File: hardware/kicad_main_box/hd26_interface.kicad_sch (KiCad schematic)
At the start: 1 part, among them J1 HD26_FEMALE

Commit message: hardware(schematic): assign exact footprints to all hierarchical schematic symbols
- Assign SMD footprints for ESP32-S3, ES8388, TCAN334G, LM5164-Q1, TPS7A0533
- Assign footprints for Bourns LM-NP-1001 transformers, TLP222A PhotoMOS, TVS, passives, and IDC26 connector
- Fix F8 PCB netlist synchronization (0 unassigned footprint errors)
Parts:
- J1: footprint (none) -> Connector_IDC:IDC-Header_2x13_P2.54mm_Vertical
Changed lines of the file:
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@@
 		(property "Reference" "J1" (at 120.0 95.0 0) (effects (font (size 1.27 1.27))))
 		(property "Value" "HD26_FEMALE" (at 120.0 98.0 0) (effects (font (size 1.27 1.27))))
+		(property "Footprint" "Connector_IDC:IDC-Header_2x13_P2.54mm_Vertical" (at 0 0 0) (effects (font (size 1.27 1.27)) (hide yes)))
 		(pin "1")
 		(pin "2")

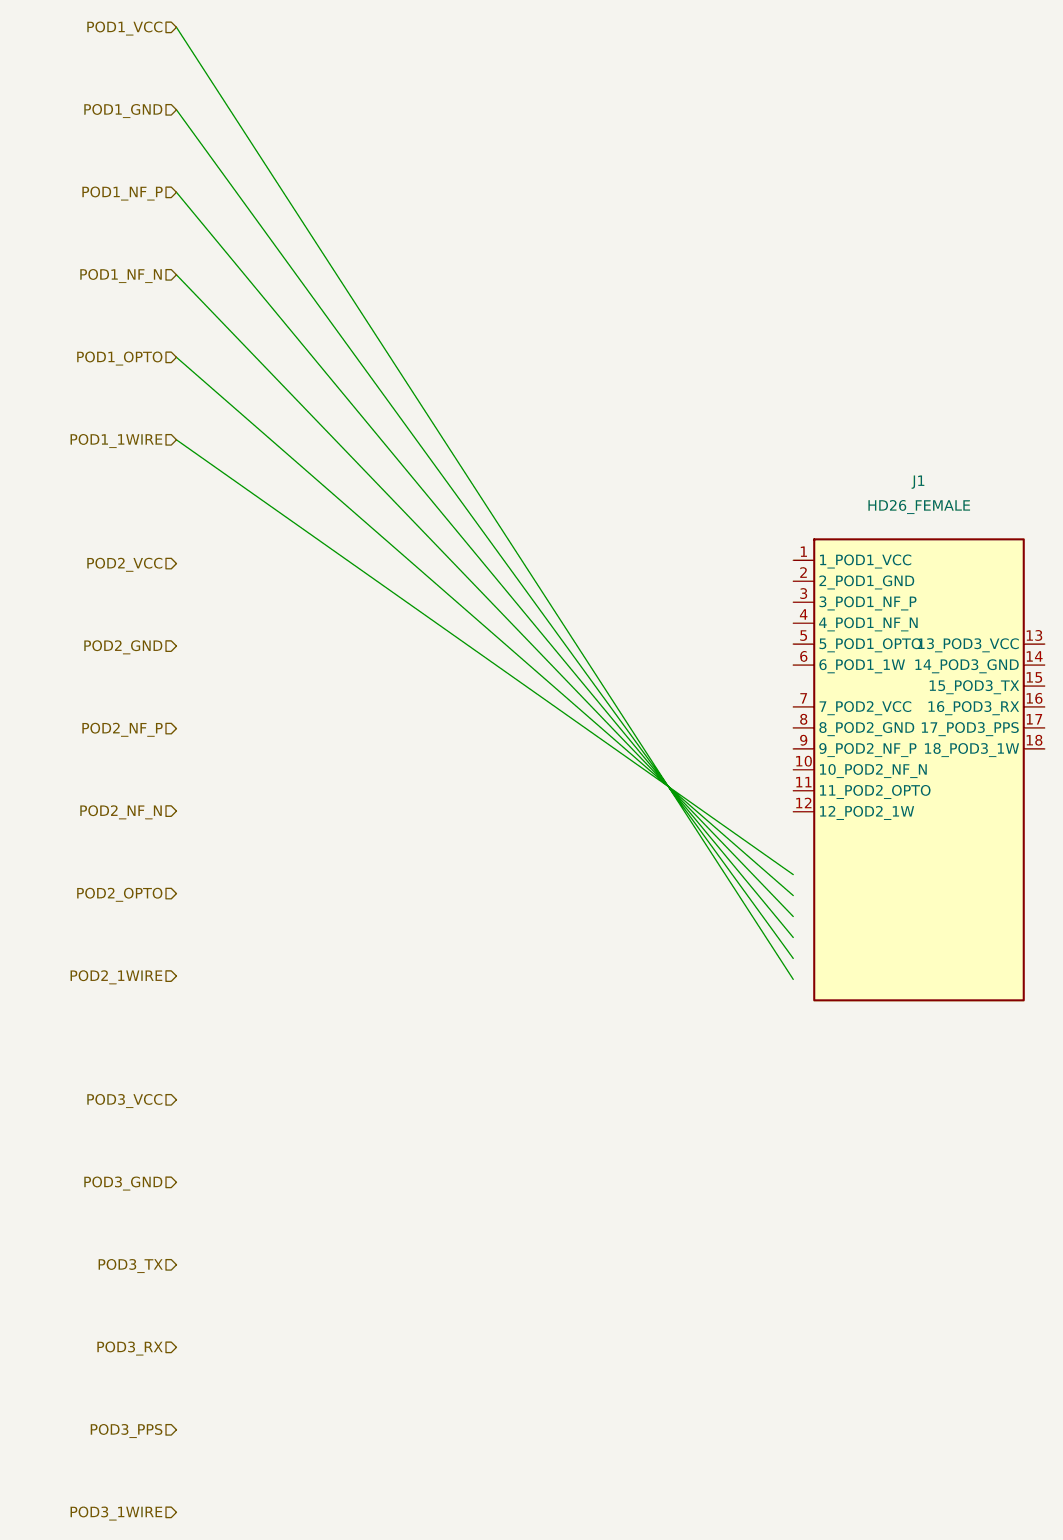
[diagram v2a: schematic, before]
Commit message: feat(arch): finalize v8.5/v9.0 Clean All-UWB Architecture, 6-PCBA lineup and Pure-DC wiring in documentation
- All-UWB Interconnects: Central Box communicates with Front-Node, Bay 1 (Left), Bay 2 (Right), and Rear Radar strictly over Qorvo DW3110 UWB (6.489 GHz Ch. 5, <0.4 ms latency, AES-128-CCM).
- Symmetrical Mounting Bays: Pod 1 and Pod 2 are physical docking bays (Bucht 1 / Bucht 2, Left / Right) for gateway units, NOT Fahrer / Sozius. Rider and pillion helmets connect directly via Bluetooth to Central Box DSP.
- 6-PCBA Lineup: PCBA 02 (Pod Base) and PCBA 04 (Rear Pod 3) retired and archived. Pod enclosures use direct 2-wire DC leaf spring contacts (+5V/GND). PCBA 03 is 2-sided SMT with DW3110, Host-MCU, and 4x AO3400A MOSFETs.
- Deutsch DTM-12 Harness: Replaced HD26 connector with 12-pin Deutsch DTM-12 automotive connector providing pure DC power.
- Power Sequencing & Roaming: Boot sequence (T=0, 200, 350, 500 ms), HW button SW1 (pairing & NVS reset), and 4-vehicle NVS roaming.
- Documentation Updated: docs/de/ 01, 03, 04, 07, 08, 09, 13, 14, 15, 16, status.md, DECISIONS_LOG.md (ADR-011), and hardware/README.md.
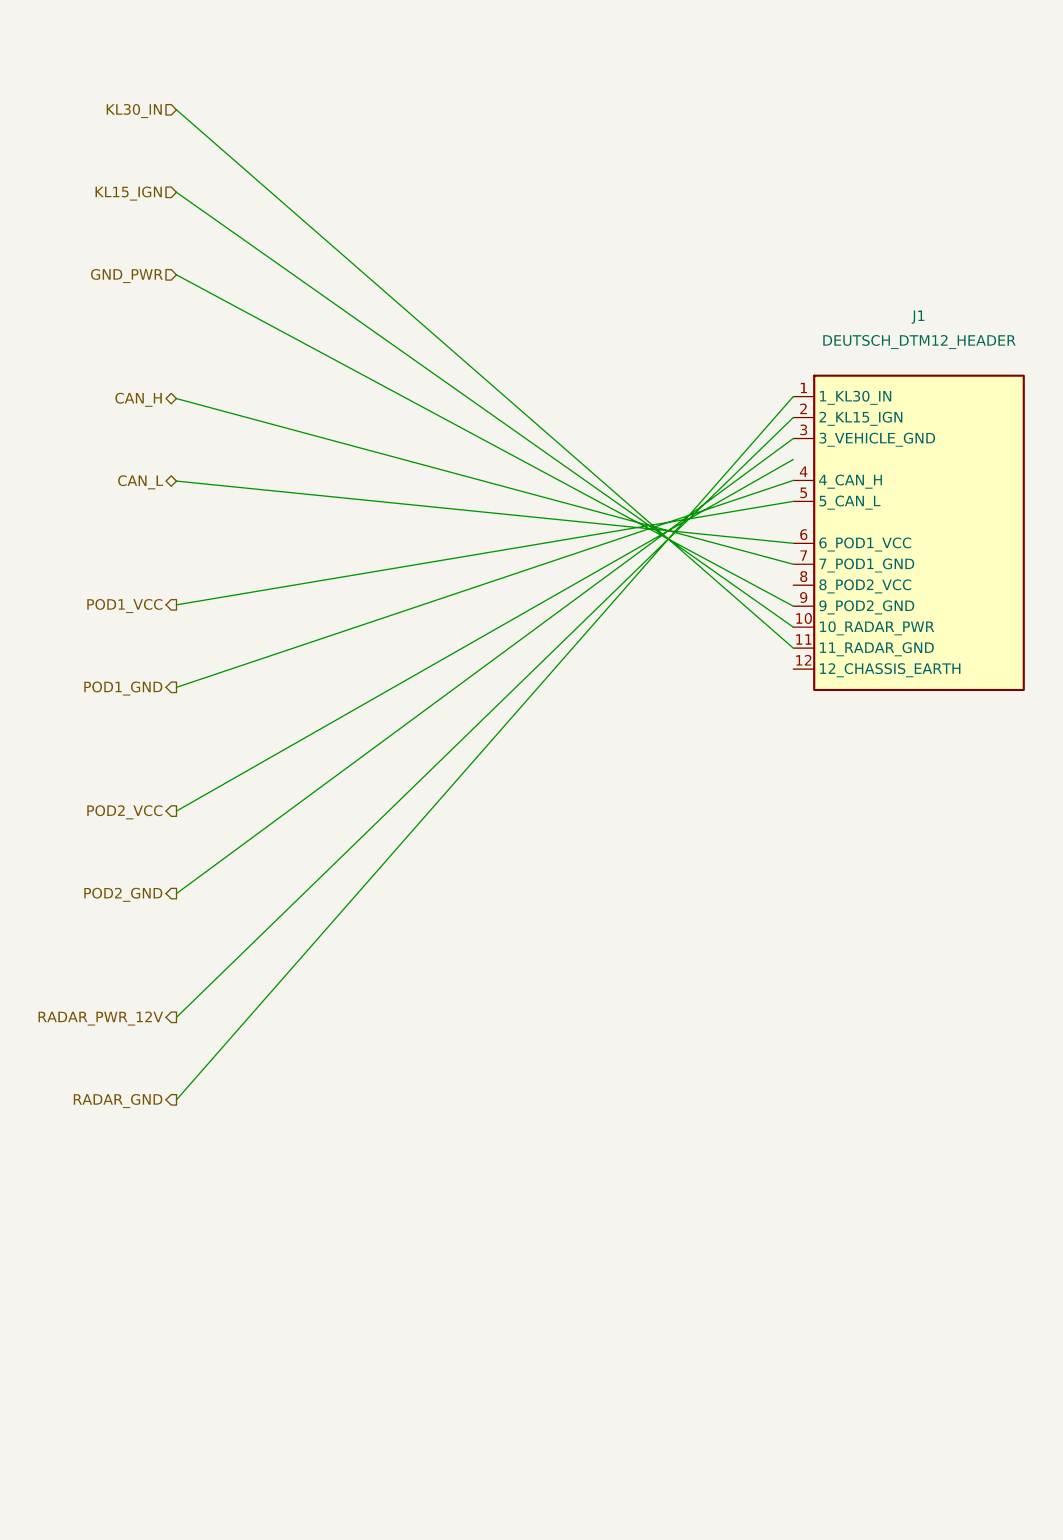
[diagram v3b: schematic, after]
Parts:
- J1: value HD26_FEMALE -> DEUTSCH_DTM12_HEADER; symbol Connector:HD26_Female -> Connector:Deutsch_DTM12_Male; LCSC (none) -> C2934175
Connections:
- net POD1_GND: now also J1.4 (4_CAN_H)
- net POD1_VCC: now also J1.5 (5_CAN_L)
- net POD2_GND: now also J1.3 (3_VEHICLE_GND)
- net RADAR_GND: now reaches J1.1 (1_KL30_IN)
- net KL15_IGN: now reaches J1.10 (10_RADAR_PWR)
- net KL30_IN: now reaches J1.11 (11_RADAR_GND)
- net RADAR_PWR_12V: now reaches J1.2 (2_KL15_IGN)
- net CAN_L: now reaches J1.6 (6_POD1_VCC)
- net CAN_H: now reaches J1.7 (7_POD1_GND)
- net GND_PWR: now reaches J1.9 (9_POD2_GND)
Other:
- title: OpenMotorBridge v8.0 - HD26 Matrix-Schnittstelle & Bordnetz -> OpenMotorBridge v8.5 / v9.0 - Deutsch DTM-12 Power & CAN Interface
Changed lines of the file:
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@@
 	(paper "A3")
 	(title_block
-		(title "OpenMotorBridge v8.0 - HD26 Matrix-Schnittstelle & Bordnetz")
-		(date "2026-08-24")
-		(rev "v8.0")
+		(title "OpenMotorBridge v8.5 / v9.0 - Deutsch DTM-12 Power & CAN Interface")
+		(date "2026-09-26")
+		(rev "v9.0")
 		(company "OpenMotorBridge Open Source Hardware")
-		(comment 1 "HD26 High-Density 26-Pin Industriesteckverbinder fuer alle externen Leitungen")
-		(comment 2 "Port 1 (Fahrer), Port 2 (Sozius), Port 3 (M8 Heck), KL30/KL15, CAN-Bus, Garmin Line-In")
+		(comment 1 "Deutsch DTM 12-Pin Automotive Industriestecker (Pure-DC & CAN)")
+		(comment 2 "KL30, KL15, GND, CAN-FD, 2x Pod 5V Power, Radar 12V Power; 100% UWB Wireless Data")
 	)
-	(hierarchical_label "POD1_VCC" (shape input) (at 30.0 40.0 180) (effects (font (size 1.27 1.27)) (justify right)))
-	(hierarchical_label "POD1_GND" (shape input) (at 30.0 50.0 180) (effects (font (size 1.27 1.27)) (justify right)))
-	(hierarchical_label "POD1_NF_P" (shape input) (at 30.0 60.0 180) (effects (font (size 1.27 1.27)) (justify right)))
-	(hierarchical_label "POD1_NF_N" (shape input) (at 30.0 70.0 180) (effects (font (size 1.27 1.27)) (justify right)))
-	(hierarchical_label "POD1_OPTO" (shape input) (at 30.0 80.0 180) (effects (font (size 1.27 1.27)) (justify right)))
-	(hierarchical_label "POD1_1WIRE" (shape input) (at 30.0 90.0 180) (effects (font (size 1.27 1.27)) (justify right)))
-	(hierarchical_label "POD2_VCC" (shape input) (at 30.0 105.0 180) (effects (font (size 1.27 1.27)) (justify right)))
-	(hierarchical_label "POD2_GND" (shape input) (at 30.0 115.0 180) (effects (font (size 1.27 1.27)) (justify right)))
-	(hierarchical_label "POD2_NF_P" (shape input) (at 30.0 125.0 180) (effects (font (size 1.27 1.27)) (justify right)))
-	(hierarchical_label "POD2_NF_N" (shape input) (at 30.0 135.0 180) (effects (font (size 1.27 1.27)) (justify right)))
-	(hierarchical_label "POD2_OPTO" (shape input) (at 30.0 145.0 180) (effects (font (size 1.27 1.27)) (justify right)))
-	(hierarchical_label "POD2_1WIRE" (shape input) (at 30.0 155.0 180) (effects (font (size 1.27 1.27)) (justify right)))
-	(hierarchical_label "POD3_VCC" (shape input) (at 30.0 170.0 180) (effects (font (size 1.27 1.27)) (justify right)))
-	(hierarchical_label "POD3_GND" (shape input) (at 30.0 180.0 180) (effects (font (size 1.27 1.27)) (justify right)))
-	(hierarchical_label "POD3_TX" (shape input) (at 30.0 190.0 180) (effects (font (size 1.27 1.27)) (justify right)))
-	(hierarchical_label "POD3_RX" (shape input) (at 30.0 200.0 180) (effects (font (size 1.27 1.27)) (justify right)))
-	(hierarchical_label "POD3_PPS" (shape input) (at 30.0 210.0 180) (effects (font (size 1.27 1.27)) (justify right)))
-	(hierarchical_label "POD3_1WIRE" (shape input) (at 30.0 220.0 180) (effects (font (size 1.27 1.27)) (justify right)))
-	(symbol (lib_id "Connector:HD26_Female") (at 120.0 130.0 0) (unit 1)
+	(hierarchical_label "KL30_IN" (shape input) (at 30.0 50.0 180) (effects (font (size 1.27 1.27)) (justify right)))
+	(hierarchical_label "KL15_IGN" (shape input) (at 30.0 60.0 180) (effects (font (size 1.27 1.27)) (justify right)))
+	(hierarchical_label "GND_PWR" (shape input) (at 30.0 70.0 180) (effects (font (size 1.27 1.27)) (justify right)))
+	(hierarchical_label "CAN_H" (shape bidirectional) (at 30.0 85.0 180) (effects (font (size 1.27 1.27)) (justify right)))
+	(hierarchical_label "CAN_L" (shape bidirectional) (at 30.0 95.0 180) (effects (font (size 1.27 1.27)) (justify right)))
+	(hierarchical_label "POD1_VCC" (shape output) (at 30.0 110.0 180) (effects (font (size 1.27 1.27)) (justify right)))
+	(hierarchical_label "POD1_GND" (shape output) (at 30.0 120.0 180) (effects (font (size 1.27 1.27)) (justify right)))
+	(hierarchical_label "POD2_VCC" (shape output) (at 30.0 135.0 180) (effects (font (size 1.27 1.27)) (justify right)))
+	(hierarchical_label "POD2_GND" (shape output) (at 30.0 145.0 180) (effects (font (size 1.27 1.27)) (justify right)))
+	(hierarchical_label "RADAR_PWR_12V" (shape output) (at 30.0 160.0 180) (effects (font (size 1.27 1.27)) (justify right)))
+	(hierarchical_label "RADAR_GND" (shape output) (at 30.0 170.0 180) (effects (font (size 1.27 1.27)) (justify right)))
+	(symbol (lib_id "Connector:Deutsch_DTM12_Male") (at 120.0 100.0 0) (unit 1)
 		(in_bom yes) (on_board yes) (dnp no)
-		(property "Reference" "J1" (at 120.0 95.0 0) (effects (font (size 1.27 1.27))))
-		(property "Value" "HD26_FEMALE" (at 120.0 98.0 0) (effects (font (size 1.27 1.27))))
+		(property "Reference" "J1" (at 120.0 75.0 0) (effects (font (size 1.27 1.27))))
+		(property "Value" "DEUTSCH_DTM12_HEADER" (at 120.0 78.0 0) (effects (font (size 1.27 1.27))))
 		(property "Footprint" "Connector_IDC:IDC-Header_2x13_P2.54mm_Vertical" (at 0 0 0) (effects (font (size 1.27 1.27)) (hide yes)))
+		(property "LCSC" "C2934175" (at 0 0 0) (effects (font (size 1.27 1.27)) (hide yes)))
 		(pin "1")
 		(pin "2")
@@
 		(pin "11")
 		(pin "12")
-		(pin "13")
-		(pin "14")
-		(pin "15")
-		(pin "16")
-		(pin "17")
-		(pin "18")
 	)
-	(wire (pts (xy 30.0 40.0) (xy 104.76 155.4)) (stroke (width 0) (type solid)))
-	(wire (pts (xy 30.0 50.0) (xy 104.76 152.86)) (stroke (width 0) (type solid)))
-	(wire (pts (xy 30.0 60.0) (xy 104.76 150.32)) (stroke (width 0) (type solid)))
-	(wire (pts (xy 30.0 70.0) (xy 104.76 147.78)) (stroke (width 0) (type solid)))
-	(wire (pts (xy 30.0 80.0) (xy 104.76 145.24)) (stroke (width 0) (type solid)))
-	(wire (pts (xy 30.0 90.0) (xy 104.76 142.7)) (stroke (width 0) (type solid)))
+	(wire (pts (xy 30.0 50.0) (xy 104.76 115.24)) (stroke (width 0) (type solid)))
+	(wire (pts (xy 30.0 60.0) (xy 104.76 112.70)) (stroke (width 0) (type solid)))
+	(wire (pts (xy 30.0 70.0) (xy 104.76 110.16)) (stroke (width 0) (type solid)))
+	(wire (pts (xy 30.0 85.0) (xy 104.76 105.08)) (stroke (width 0) (type solid)))
+	(wire (pts (xy 30.0 95.0) (xy 104.76 102.54)) (stroke (width 0) (type solid)))
+	(wire (pts (xy 30.0 110.0) (xy 104.76 97.46)) (stroke (width 0) (type solid)))
+	(wire (pts (xy 30.0 120.0) (xy 104.76 94.92)) (stroke (width 0) (type solid)))
+	(wire (pts (xy 30.0 135.0) (xy 104.76 92.38)) (stroke (width 0) (type solid)))
+	(wire (pts (xy 30.0 145.0) (xy 104.76 89.84)) (stroke (width 0) (type solid)))
+	(wire (pts (xy 30.0 160.0) (xy 104.76 87.30)) (stroke (width 0) (type solid)))
+	(wire (pts (xy 30.0 170.0) (xy 104.76 84.76)) (stroke (width 0) (type solid)))
 )

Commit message: hardware(pcb): synchronize 5-PCBA lineup with v9.6 All-UWB architecture
- PCBA 01 (Central Box): replace obsolete 26-pin IDC header with 12-pin Deutsch DTM-12 header (exact 12-pin net mapping), add 38.4MHz UWB crystal on B.Cu, update silkscreen and schematic
- PCBA 05 (Front Node): place Qorvo DW3110 + U.FL + crystal on B.Cu; place u-blox SAM-M10Q GNSS + Knowles MEMS mic on F.Cu
- PCBA 03 (Pod Cartridge): replace obsolete 6-pin dock socket with PAD1/PAD2 DC spring contact pads; place DW3110 + U.FL on B.Cu
- PCBA 08 (Radar Sub-MCU): update J1 to 2-pin 12V automotive power connector; place DW3110 + U.FL on B.Cu
- PCBA 07 (Smart Keyfob): replace solder pads with 2-pin JST-ACH SMD header (J_QI) for solderless Qi coil connection
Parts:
- J1: footprint Connector_IDC:IDC-Header_2x13_P2.54mm_Vertical -> Connector_PinHeader_2.54mm:PinHeader_2x06_P2.54mm_Vertical
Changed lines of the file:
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@@
 		(property "Reference" "J1" (at 120.0 75.0 0) (effects (font (size 1.27 1.27))))
 		(property "Value" "DEUTSCH_DTM12_HEADER" (at 120.0 78.0 0) (effects (font (size 1.27 1.27))))
-		(property "Footprint" "Connector_IDC:IDC-Header_2x13_P2.54mm_Vertical" (at 0 0 0) (effects (font (size 1.27 1.27)) (hide yes)))
+		(property "Footprint" "Connector_PinHeader_2.54mm:PinHeader_2x06_P2.54mm_Vertical" (at 0 0 0) (effects (font (size 1.27 1.27)) (hide yes)))
 		(property "LCSC" "C2934175" (at 0 0 0) (effects (font (size 1.27 1.27)) (hide yes)))
 		(pin "1")

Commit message: hardware(main-box): replace J1 open pinheader with official shrouded IDC box header (Wannenstecker)
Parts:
- J1: footprint Connector_PinHeader_2.54mm:PinHeader_2x06_P2.54mm_Vertical -> Connector_IDC:IDC-Header_2x06_P2.54mm_Vertical
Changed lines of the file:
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@@
 		(property "Reference" "J1" (at 120.0 75.0 0) (effects (font (size 1.27 1.27))))
 		(property "Value" "DEUTSCH_DTM12_HEADER" (at 120.0 78.0 0) (effects (font (size 1.27 1.27))))
-		(property "Footprint" "Connector_PinHeader_2.54mm:PinHeader_2x06_P2.54mm_Vertical" (at 0 0 0) (effects (font (size 1.27 1.27)) (hide yes)))
+		(property "Footprint" "Connector_IDC:IDC-Header_2x06_P2.54mm_Vertical" (at 0 0 0) (effects (font (size 1.27 1.27)) (hide yes)))
 		(property "LCSC" "C2934175" (at 0 0 0) (effects (font (size 1.27 1.27)) (hide yes)))
 		(pin "1")
